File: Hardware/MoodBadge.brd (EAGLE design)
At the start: 160 x 100 mm, 1 part

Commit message: EAGLE files
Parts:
- removed D1: 15KEXX, diode:CB429-17
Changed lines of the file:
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@@
 </autorouter>
 <elements>
-<element name="D1" library="diode" library_urn="urn:adsk.eagle:library:210" package="CB429-17" package3d_urn="urn:adsk.eagle:package:43360/1" value="15KEXX" x="11.43" y="-5.08" smashed="yes">
-<attribute name="NAME" x="6.35" y="-2.159" size="1.27" layer="25" ratio="10"/>
-<attribute name="VALUE" x="8.89" y="-7.239" size="1.27" layer="27" ratio="10"/>
-</element>
 </elements>
 <signals>
@@
 </board>
 </drawing>
-<compatibility>
-<note version="8.2" severity="warning">
-Since Version 8.2, EAGLE supports online libraries. The ids
-of those online libraries will not be understood (or retained)
-with this version.
-</note>
-<note version="8.3" severity="warning">
-Since Version 8.3, EAGLE supports URNs for individual library
-assets (packages, symbols, and devices). The URNs of those assets
-will not be understood (or retained) with this version.
-</note>
-<note version="8.3" severity="warning">
-Since Version 8.3, EAGLE supports the association of 3D packages
-with devices in libraries, schematics, and board files. Those 3D
-packages will not be understood (or retained) with this version.
-</note>
-</compatibility>
 </eagle>

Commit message: Created board outline and started schematic
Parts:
- added C1, C8, C9: 4.7uF, SparkFun-Capacitors:0603
- added C2, C3, C4, C5, C6, C7: 100n, LinnesLab-Passives:C0603
- added D1, D2: 1A/23V/620mV, LinnesLab-DiscreteSemi:USC
- added DOWN, LEFT, MODE, RIGHT, SELECT, UP: (no value), LinnesLab-Switches:SPST.KT11P4SM34LFS
- added LED1, LED2, LED3, LED4, LED5, LED6, LED7: (no value), LinnesLab-LED:LED-0603
- added LIPO: (no value), LinnesLab-Connectors:JST-2-SMD
- added ON/OFF: SWITCH.JS202011JXQNUPWARDS, LinnesLab-Switches:SWITCH.00
- added R1, R11, R3, R5, R7, R9: 10k, LinnesLab-Passives:R0603
- added R10, R12, R13, R14, R2, R4, R6, R8: 1k, LinnesLab-Passives:R0603
- added U1: MCP73831, SparkFun-IC-Power:SOT23-5
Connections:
- new net DOWN: C4.1, DOWN.3, DOWN.4, R5.2, R6.2
- new net GND: C1.2, C2.2, C3.2, C4.2, C5.2, C6.2, C7.2, C9.2, LED1.C, LED2.C, LED3.C, LED4.C, LED5.C, LED6.C, LIPO.1, R1.1, R11.1, R14.1, R3.1, R5.1, R7.1, R9.1, U1.2
- new net LEFT: C2.1, LEFT.3, LEFT.4, R1.2, R2.2
- new net MODE: C7.1, MODE.3, MODE.4, R11.2, R12.2
- new net N$11: LED5.A, R10.1
- new net N$13: LED6.A, R12.1
- new net N$2: D1.+, ON/OFF.1
- new net N$3: LED1.A, R2.1
- new net N$4: R14.2, U1.5
- new net N$5: LED2.A, R4.1
- new net N$7: LED3.A, R6.1
- new net N$9: LED4.A, R8.1
- new net RIGHT: C6.1, R10.2, R9.2, RIGHT.3, RIGHT.4
- new net SELECT: C3.1, R3.2, R4.2, SELECT.3, SELECT.4
- new net UP: C5.1, R7.2, R8.2, UP.3, UP.4
- new net VCC: DOWN.1, DOWN.2, LEFT.1, LEFT.2, MODE.1, MODE.2, RIGHT.1, RIGHT.2, SELECT.1, SELECT.2, UP.1, UP.2
- new net VIN: U1.4
- new net VLIPO: C1.1, C9.1, D1.-, LIPO.2, ON/OFF.2, U1.3
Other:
- board size 160 x 100 mm -> 195.6 x 195.6 mm

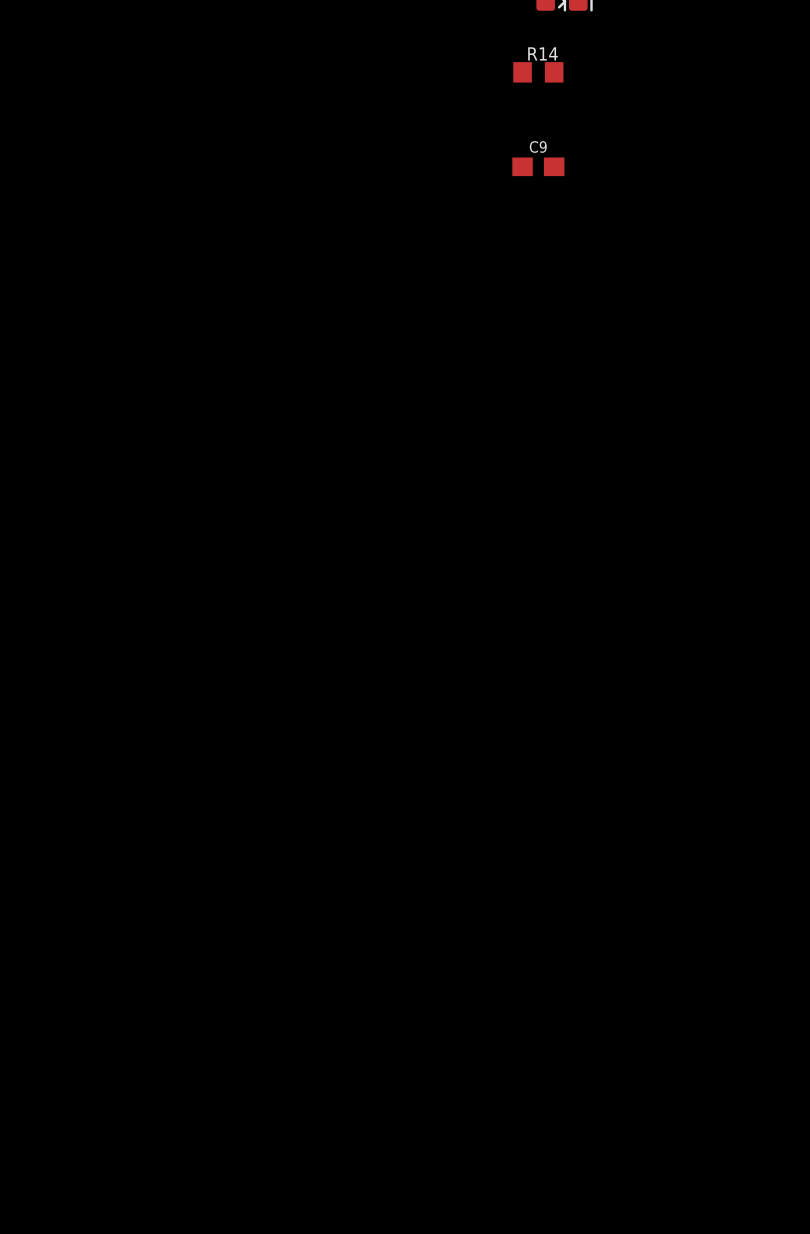
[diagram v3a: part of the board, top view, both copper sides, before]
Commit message: Added battery charger and microcontroller sections
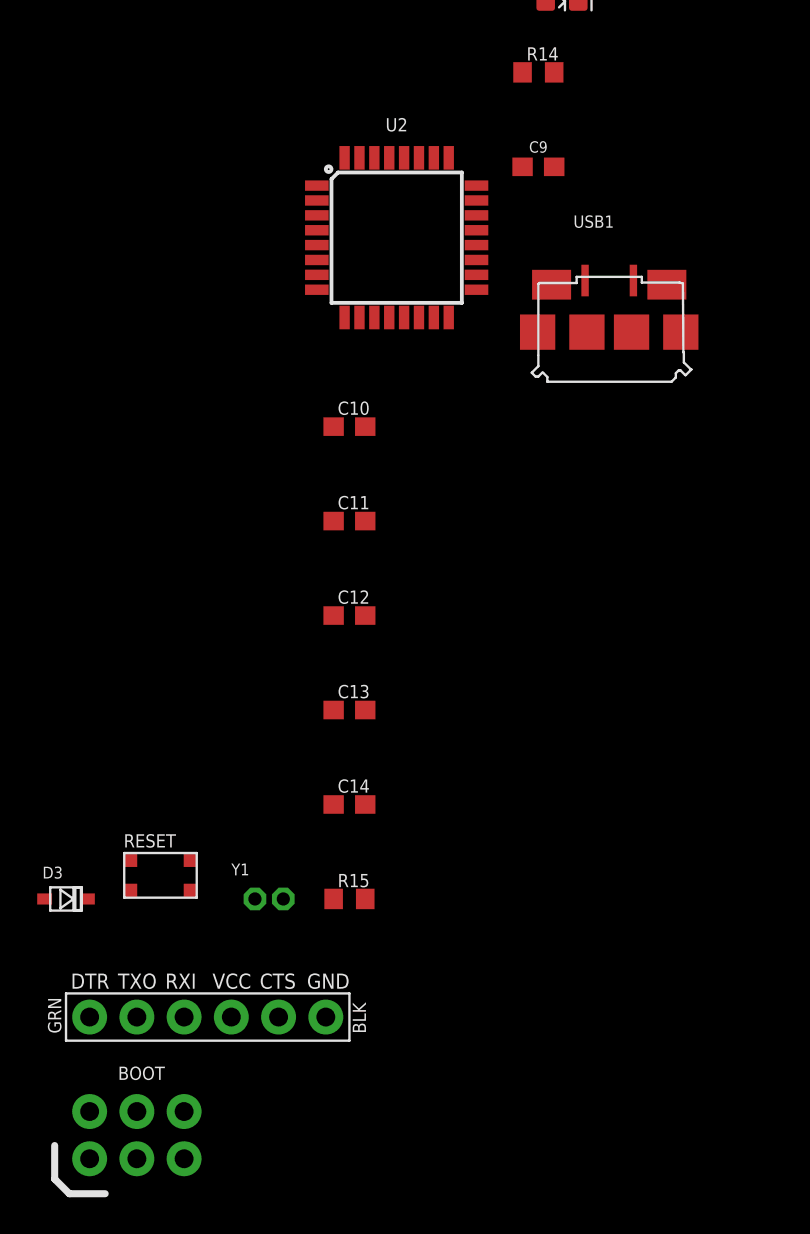
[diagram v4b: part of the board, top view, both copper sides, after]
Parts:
- added BOOT: AVR_SPI_PROG_3X2NS, LinnesLab-Connectors:2X3-NS
- added C10: 2.2u, LinnesLab-Passives:C0603
- added C11, C14: 0.1u, LinnesLab-Passives:C0603
- added C12, C13: 22p, LinnesLab-Passives:C0603
- added D3: 1A/23V/620mV, LinnesLab-DiscreteSemi:USC
- added FTDI1: FTDI_DEVICE, LinnesLab-Connectors:FTDI_DEVICE
- added R15: 10k, LinnesLab-Passives:R0603
- added RESET: (no value), LinnesLab-Switches:BUTTON-GULLWING
- added U2: ATMEGA328P_TQFP, LinnesLab-Microcontrollers:TQFP32-08
- added USB1: USB.MICRO.PWR-BIGGERPADS, LinnesLab-Connectors:USB-MICRO-01.BIGGERPADS.PWR
- added Y1: (no value), LinnesLab-Clocks:CA-301
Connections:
- removed net VIN: U1.4
- new net DTR: C14.1, FTDI1.GND
- new net LD1: U2.2
- new net LD10: BOOT.1, U2.16
- new net LD11: BOOT.4, U2.15
- new net LD12: U2.14
- new net LD13: U2.13
- new net LD14: U2.12
- new net LD15: U2.11
- new net LD16: U2.10
- new net LD2: U2.1
- new net LD3: U2.32
- new net LD4: U2.28
- new net LD5: U2.27
- new net LD6: U2.26
- new net LD9: BOOT.3, U2.17
- new net N$1: D2.+, USB1.1
- new net N$10: C12.1, U2.8, Y1.1
- new net N$12: D3.+, FTDI1.RXI
- new net N$6: LED7.A, R13.1
- new net N$8: C13.1, U2.7, Y1.2
- new net RESET: BOOT.5, C14.2, R15.1, RESET.1, RESET.2, U2.29
- new net RXD: FTDI1.CTS, U2.30
- new net STAT: LED7.C, U1.1
- new net TXD: FTDI1.VCC, U2.31
- net DOWN: now also U2.25
- net GND: now also BOOT.6, C10.2, C11.2, C12.2, C13.2, C8.2, FTDI1.DTR, FTDI1.TXO, RESET.3, RESET.4, U2.21, U2.3, U2.5, USB1.5
- net LEFT: now also U2.23
- net MODE: now also U2.9
- net RIGHT: now also U2.22
- net SELECT: now also U2.19
- net UP: now also U2.24
- net VCC: now also BOOT.2, C10.1, C11.1, C8.1, D2.-, D3.-, R13.2, R15.2, U1.4, U2.18, U2.4, U2.6

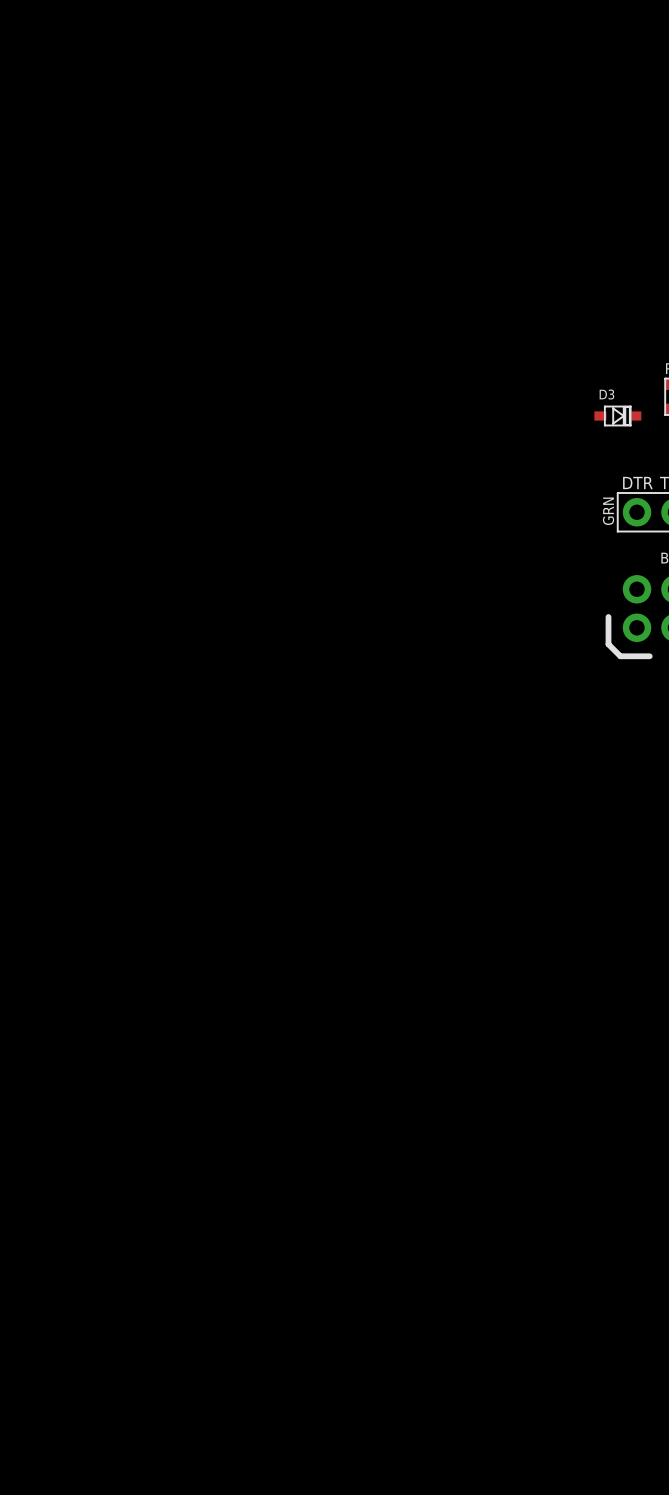
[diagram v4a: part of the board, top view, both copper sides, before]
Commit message: Added LED matrix and fixed Arduino output pins
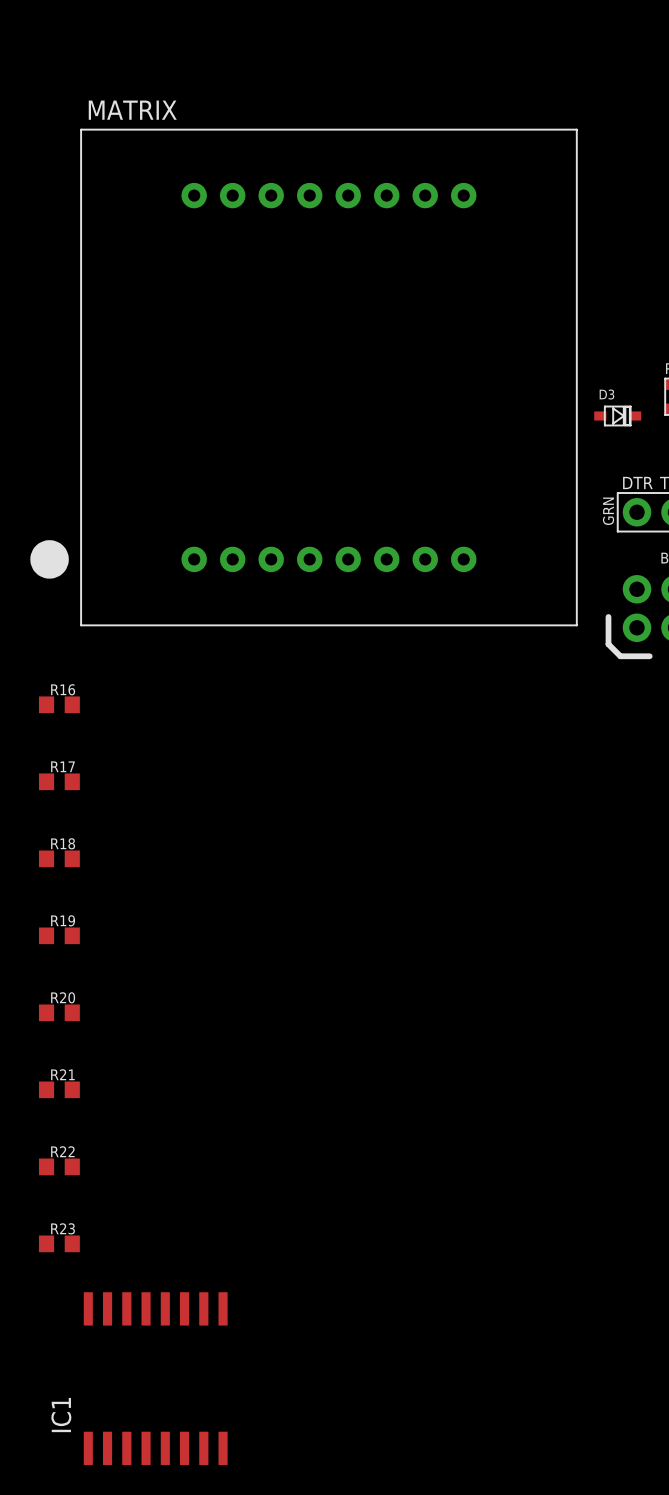
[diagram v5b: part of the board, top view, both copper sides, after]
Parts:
- added IC1: PCF8574T, micro-philips:SO16W
- added MATRIX: (no value), adafruit:SEGMENT_BL-M12A883
- added R16, R17, R18, R19, R20, R21, R22, R23: 205, LinnesLab-Passives:R0603
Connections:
- new net LD7: R21.1, U2.25
- new net LD8: R18.1, U2.24
- new net N$14: MATRIX.9, R16.2
- new net N$15: MATRIX.14, R17.2
- new net N$16: MATRIX.8, R18.2
- new net N$17: MATRIX.12, R19.2
- new net N$18: MATRIX.1, R20.2
- new net N$19: MATRIX.7, R21.2
- new net N$20: MATRIX.2, R22.2
- new net N$21: MATRIX.5, R23.2
- new net SCL: IC1.14, U2.28
- new net SDA: IC1.15, U2.27
- net DOWN: now also IC1.5; no longer U2.25
- net GND: now also IC1.8
- net LD1: now also R20.1
- net LD10: now also MATRIX.10
- net LD11: now also MATRIX.11
- net LD12: now also R19.1
- net LD13: now also MATRIX.13
- net LD14: now also R17.1
- net LD15: now also MATRIX.15
- net LD16: now also MATRIX.16
- net LD2: now also R22.1
- net LD3: now also MATRIX.3
- net LD4: now also MATRIX.4; no longer U2.28
- net LD5: now also R23.1; no longer U2.27
- net LD6: now also MATRIX.6
- net LD9: now also R16.1
- net LEFT: now also IC1.6; no longer U2.23
- net MODE: now also IC1.10
- net RIGHT: now also IC1.7; no longer U2.22
- net SELECT: now also IC1.9; no longer U2.19
- net UP: now also IC1.4; no longer U2.24
- net VCC: now also IC1.16

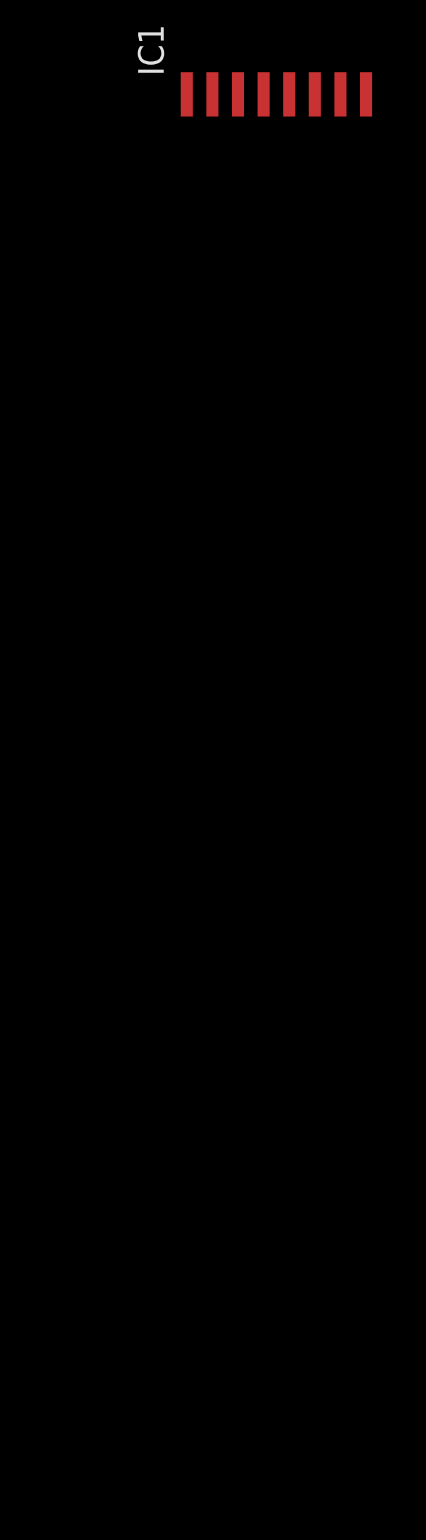
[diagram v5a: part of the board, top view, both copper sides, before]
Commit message: Added remaining parts of circuit and port expander. Connected Pulse pin
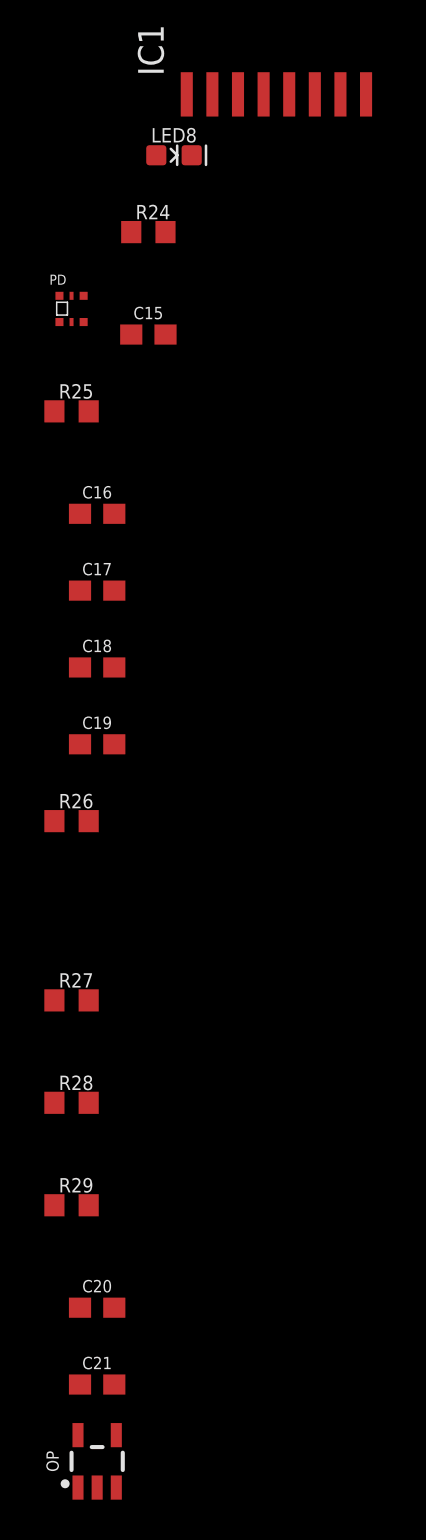
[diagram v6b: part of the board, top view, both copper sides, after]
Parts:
- added C15, C21: 100n, SparkFun-Capacitors:0603
- added C16, C17, C18: 4.7u, SparkFun-Capacitors:0603
- added C19: 2.2u, SparkFun-Capacitors:0603
- added C20: 1u, SparkFun-Capacitors:0603
- added LED8: (no value), LinnesLab-LED:LED-0603
- added OP: OP-SINGLEOT, LinnesLab-AnalogIC:SOT23-5
- added PD: ADPS9008, LinnesLab-Sensors:6-PIN.CHIPLED
- added R24: 487, LinnesLab-Passives:R0603
- added R25: 12k, LinnesLab-Passives:R0603
- added R26: 10k, LinnesLab-Passives:R0603
- added R27: 3.3M, LinnesLab-Passives:R0603
- added R28, R29: 210k, LinnesLab-Passives:R0603
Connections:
- new net N$22: LED8.C, R24.2
- new net N$23: C17.1, PD.6, R25.2
- new net N$24: C16.1, C17.2, C18.1
- new net N$25: C19.2, OP.3, R28.1, R29.2
- new net N$26: C18.2, C19.1, R26.1
- new net N$28: OP.4, R26.2, R27.1
- new net PULSE: OP.1, R27.2, U2.10
- net GND: now also C15.2, C16.2, C20.1, C21.2, OP.2, PD.4, R24.1, R25.1, R29.1
- net LD16: now also U2.9; no longer U2.10
- net MODE: no longer U2.9
- net VCC: now also C15.1, C20.2, C21.1, LED8.A, OP.5, PD.1, R28.2
